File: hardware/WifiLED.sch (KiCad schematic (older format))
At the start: 22 parts, among them P1 CONN_01X03, P2 CONN_01X03, P3 CONN_01X01, P4 CONN_01X01, P5 CONN_01X01, P6 CONN_01X01

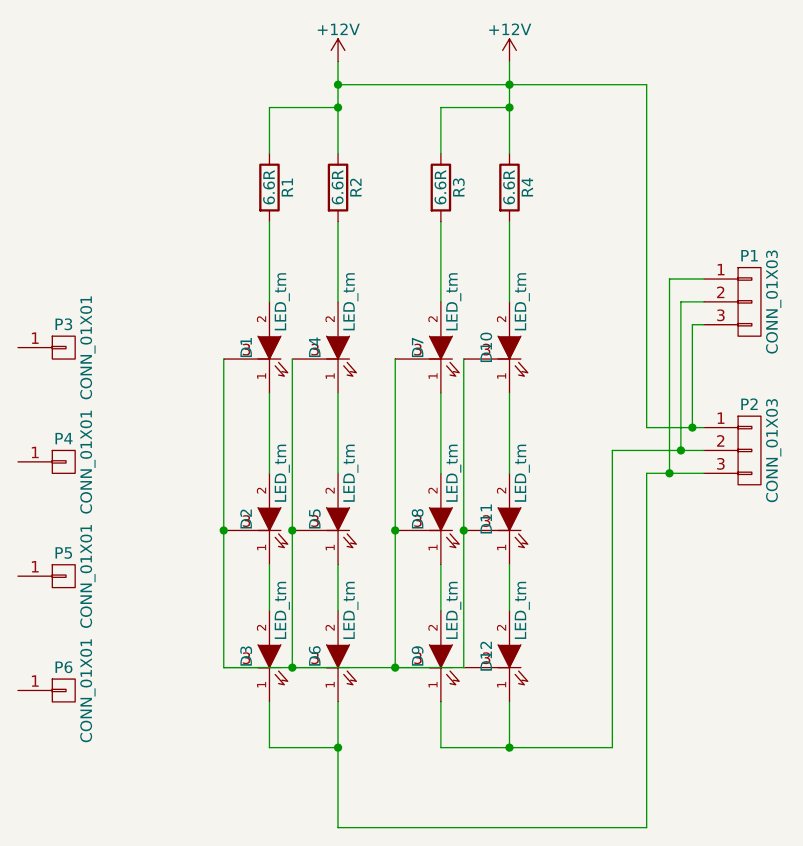
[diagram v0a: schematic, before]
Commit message: Removed libopencm3 and software
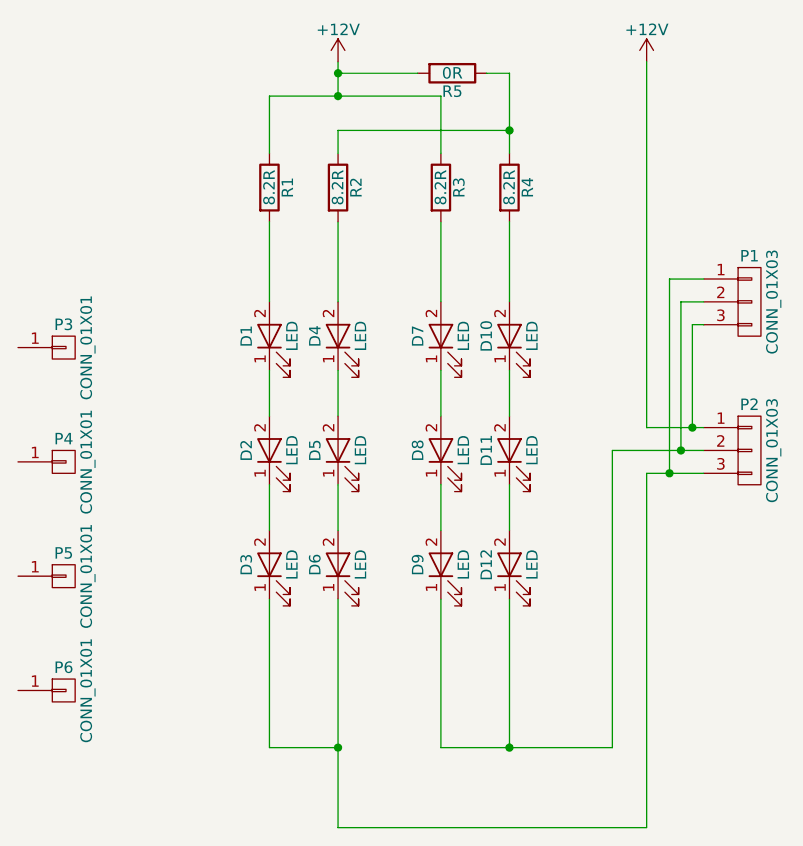
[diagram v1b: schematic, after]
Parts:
- removed D1, D10, D11, D12, D2, D3, D4, D5, D6, D7, D8, D9: LED_tm, matthew:CREE_MX6, symbol LED_tm
- added D1, D10, D11, D12, D2, D3, D4, D5, D6, D7, D8, D9: LED, matthew:LED3030, symbol LED
- added R5: 0R, Resistors_SMD:R_2512, symbol R
- R1, R2, R3, R4: value 6.6R -> 8.2R; footprint Resistors_SMD:R_2512_HandSoldering -> Resistors_SMD:R_2512
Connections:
- net +12V: now also R5.2; no longer R2.1, R4.1
- net at R2.2: now also D4.2 (A)
- net at R1.2: now also D1.2 (A)
- net at R4.2: now also D10.2 (A)
- net at R3.2: now also D7.2 (A)
- net at P1.2 (P2), P2.2 (P2): now also D12.1 (K), D9.1 (K)
- net at P1.1 (P1), P2.3 (P3): now also D3.1 (K), D6.1 (K)
- new net: R2.1, R4.1, R5.1
- new net: D10.1 (K), D11.2 (A)
- new net: D11.1 (K), D12.2 (A)
- new net: D7.1 (K), D8.2 (A)
- new net: D8.1 (K), D9.2 (A)
- new net: D4.1 (K), D5.2 (A)
- new net: D5.1 (K), D6.2 (A)
- new net: D1.1 (K), D2.2 (A)
- new net: D2.1 (K), D3.2 (A)
